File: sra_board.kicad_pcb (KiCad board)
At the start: 2 copper layers, 1 part, among them U2 ESP32-WROOM-32E

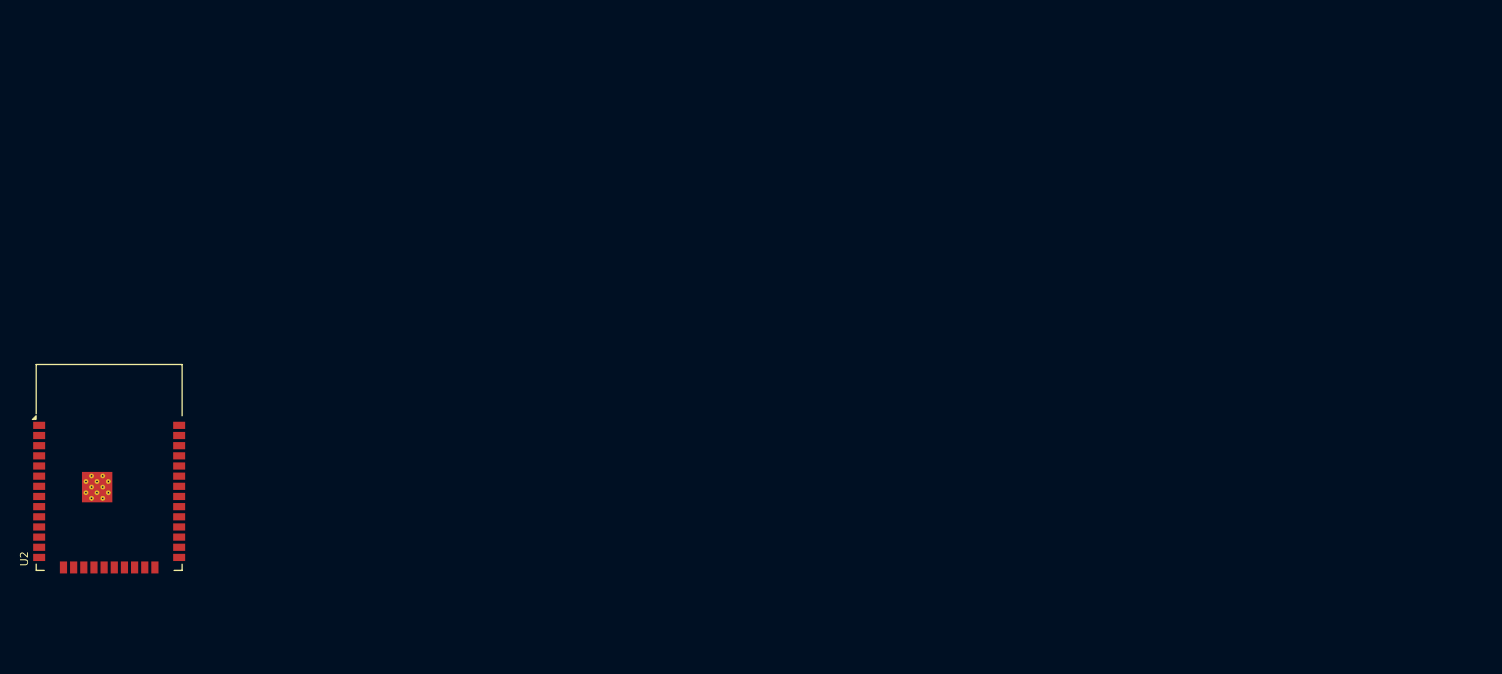
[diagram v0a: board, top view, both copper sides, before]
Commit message: Added Boot circuit and USB-to-TTL
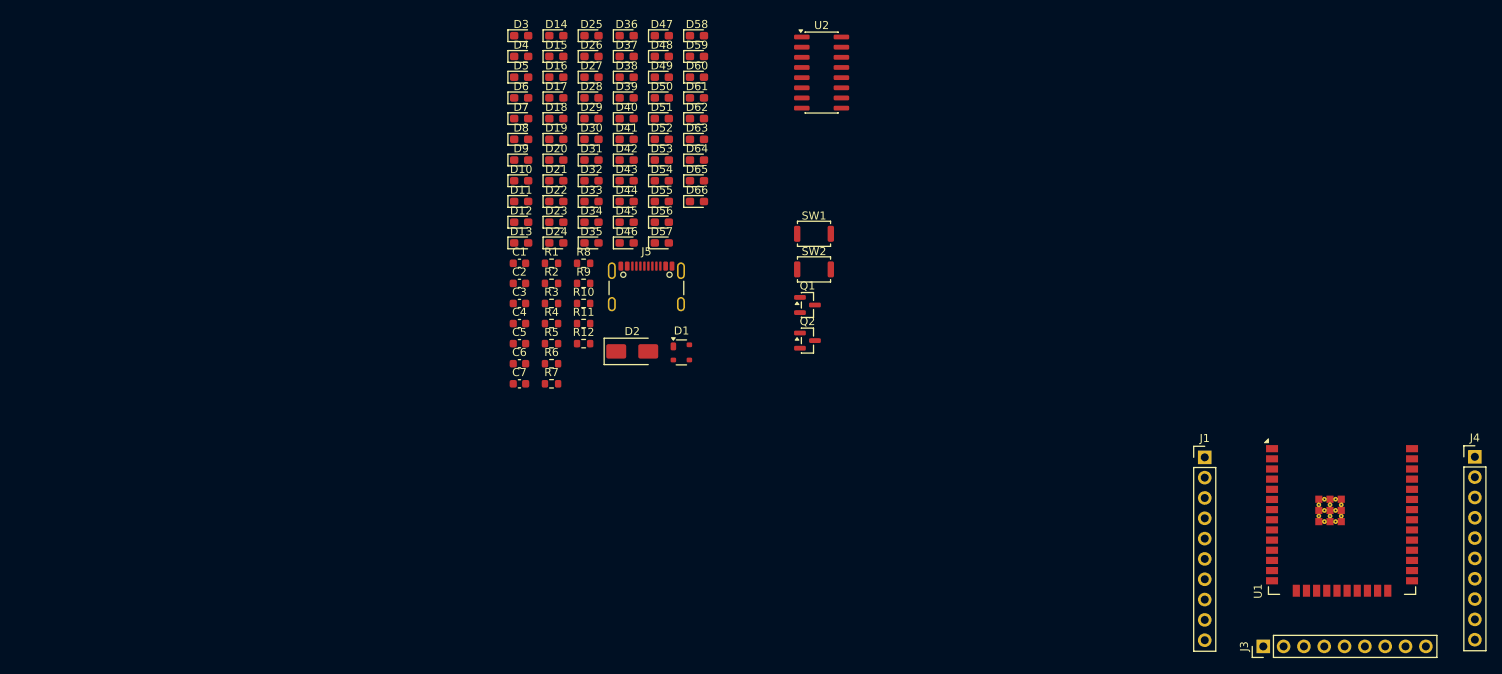
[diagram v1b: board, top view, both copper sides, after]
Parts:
- added C1: 0.1uf, Capacitor_SMD:C_0603_1608Metric, F.Cu at (105.5, 42.1)
- added C2: 0.1uF, Capacitor_SMD:C_0603_1608Metric, F.Cu at (105.5, 44.6)
- added C3: 0.1 uF, Capacitor_SMD:C_0603_1608Metric, F.Cu at (105.5, 47.1)
- added C4: 0.1uF, Capacitor_SMD:C_0603_1608Metric, F.Cu at (105.5, 49.6)
- added C5: 0.1uF, Capacitor_SMD:C_0603_1608Metric, F.Cu at (105.5, 52.1)
- added C6: 100nf, Capacitor_SMD:C_0603_1608Metric, F.Cu at (105.5, 54.6)
- added C7: 10uf, Capacitor_SMD:C_0603_1608Metric, F.Cu at (105.5, 57.1)
- added D1: SP0503BAHT, Package_TO_SOT_SMD:SOT-143, F.Cu at (125.7, 53.2)
- added D10: LED, LED_SMD:LED_0603_1608Metric_Pad1.05x0.95mm_HandSolder, F.Cu at (105.7, 31.7)
- added D11: LED, LED_SMD:LED_0603_1608Metric_Pad1.05x0.95mm_HandSolder, F.Cu at (105.7, 34.3)
- added D12: LED, LED_SMD:LED_0603_1608Metric_Pad1.05x0.95mm_HandSolder, F.Cu at (105.7, 36.9)
- added D13: LED, LED_SMD:LED_0603_1608Metric_Pad1.05x0.95mm_HandSolder, F.Cu at (105.7, 39.5)
- added D14: LED, LED_SMD:LED_0603_1608Metric_Pad1.05x0.95mm_HandSolder, F.Cu at (110.1, 13.6)
- added D15: LED, LED_SMD:LED_0603_1608Metric_Pad1.05x0.95mm_HandSolder, F.Cu at (110.1, 16.2)
- added D16: LED, LED_SMD:LED_0603_1608Metric_Pad1.05x0.95mm_HandSolder, F.Cu at (110.1, 18.8)
- added D17: LED, LED_SMD:LED_0603_1608Metric_Pad1.05x0.95mm_HandSolder, F.Cu at (110.1, 21.4)
- added D18: LED, LED_SMD:LED_0603_1608Metric_Pad1.05x0.95mm_HandSolder, F.Cu at (110.1, 24.0)
- added D19: LED, LED_SMD:LED_0603_1608Metric_Pad1.05x0.95mm_HandSolder, F.Cu at (110.1, 26.6)
- added D2: SS14, Diode_SMD:D_SMA, F.Cu at (119.6, 53.1)
- added D20: LED, LED_SMD:LED_0603_1608Metric_Pad1.05x0.95mm_HandSolder, F.Cu at (110.1, 29.2)
- added D21: LED, LED_SMD:LED_0603_1608Metric_Pad1.05x0.95mm_HandSolder, F.Cu at (110.1, 31.7)
- added D22: LED, LED_SMD:LED_0603_1608Metric_Pad1.05x0.95mm_HandSolder, F.Cu at (110.1, 34.3)
- added D23: LED, LED_SMD:LED_0603_1608Metric_Pad1.05x0.95mm_HandSolder, F.Cu at (110.1, 36.9)
- added D24: LED, LED_SMD:LED_0603_1608Metric_Pad1.05x0.95mm_HandSolder, F.Cu at (110.1, 39.5)
- added D25: LED, LED_SMD:LED_0603_1608Metric_Pad1.05x0.95mm_HandSolder, F.Cu at (114.5, 13.6)
- added D26: LED, LED_SMD:LED_0603_1608Metric_Pad1.05x0.95mm_HandSolder, F.Cu at (114.5, 16.2)
- added D27: LED, LED_SMD:LED_0603_1608Metric_Pad1.05x0.95mm_HandSolder, F.Cu at (114.5, 18.8)
- added D28: LED, LED_SMD:LED_0603_1608Metric_Pad1.05x0.95mm_HandSolder, F.Cu at (114.5, 21.4)
- added D29: LED, LED_SMD:LED_0603_1608Metric_Pad1.05x0.95mm_HandSolder, F.Cu at (114.5, 24.0)
- added D3: LED, LED_SMD:LED_0603_1608Metric_Pad1.05x0.95mm_HandSolder, F.Cu at (105.7, 13.6)
- added D30: LED, LED_SMD:LED_0603_1608Metric_Pad1.05x0.95mm_HandSolder, F.Cu at (114.5, 26.6)
- added D31: LED, LED_SMD:LED_0603_1608Metric_Pad1.05x0.95mm_HandSolder, F.Cu at (114.5, 29.2)
- added D32: LED, LED_SMD:LED_0603_1608Metric_Pad1.05x0.95mm_HandSolder, F.Cu at (114.5, 31.7)
- added D33: LED, LED_SMD:LED_0603_1608Metric_Pad1.05x0.95mm_HandSolder, F.Cu at (114.5, 34.3)
- added D34: LED, LED_SMD:LED_0603_1608Metric_Pad1.05x0.95mm_HandSolder, F.Cu at (114.5, 36.9)
- added D35: LED, LED_SMD:LED_0603_1608Metric_Pad1.05x0.95mm_HandSolder, F.Cu at (114.5, 39.5)
- added D36: LED, LED_SMD:LED_0603_1608Metric_Pad1.05x0.95mm_HandSolder, F.Cu at (118.9, 13.6)
- added D37: LED, LED_SMD:LED_0603_1608Metric_Pad1.05x0.95mm_HandSolder, F.Cu at (118.9, 16.2)
- added D38: LED, LED_SMD:LED_0603_1608Metric_Pad1.05x0.95mm_HandSolder, F.Cu at (118.9, 18.8)
- added D39: LED, LED_SMD:LED_0603_1608Metric_Pad1.05x0.95mm_HandSolder, F.Cu at (118.9, 21.4)
- added D4: LED, LED_SMD:LED_0603_1608Metric_Pad1.05x0.95mm_HandSolder, F.Cu at (105.7, 16.2)
- added D40: LED, LED_SMD:LED_0603_1608Metric_Pad1.05x0.95mm_HandSolder, F.Cu at (118.9, 24.0)
- added D41: LED, LED_SMD:LED_0603_1608Metric_Pad1.05x0.95mm_HandSolder, F.Cu at (118.9, 26.6)
- added D42: LED, LED_SMD:LED_0603_1608Metric_Pad1.05x0.95mm_HandSolder, F.Cu at (118.9, 29.2)
- added D43: LED, LED_SMD:LED_0603_1608Metric_Pad1.05x0.95mm_HandSolder, F.Cu at (118.9, 31.7)
- added D44: LED, LED_SMD:LED_0603_1608Metric_Pad1.05x0.95mm_HandSolder, F.Cu at (118.9, 34.3)
- added D45: LED, LED_SMD:LED_0603_1608Metric_Pad1.05x0.95mm_HandSolder, F.Cu at (118.9, 36.9)
- added D46: LED, LED_SMD:LED_0603_1608Metric_Pad1.05x0.95mm_HandSolder, F.Cu at (118.9, 39.5)
- added D47: LED, LED_SMD:LED_0603_1608Metric_Pad1.05x0.95mm_HandSolder, F.Cu at (123.3, 13.6)
- added D48: LED, LED_SMD:LED_0603_1608Metric_Pad1.05x0.95mm_HandSolder, F.Cu at (123.3, 16.2)
- added D49: LED, LED_SMD:LED_0603_1608Metric_Pad1.05x0.95mm_HandSolder, F.Cu at (123.3, 18.8)
- added D5: LED, LED_SMD:LED_0603_1608Metric_Pad1.05x0.95mm_HandSolder, F.Cu at (105.7, 18.8)
- added D50: LED, LED_SMD:LED_0603_1608Metric_Pad1.05x0.95mm_HandSolder, F.Cu at (123.3, 21.4)
- added D51: LED, LED_SMD:LED_0603_1608Metric_Pad1.05x0.95mm_HandSolder, F.Cu at (123.3, 24.0)
- added D52: LED, LED_SMD:LED_0603_1608Metric_Pad1.05x0.95mm_HandSolder, F.Cu at (123.3, 26.6)
- added D53: LED, LED_SMD:LED_0603_1608Metric_Pad1.05x0.95mm_HandSolder, F.Cu at (123.3, 29.2)
- added D54: LED, LED_SMD:LED_0603_1608Metric_Pad1.05x0.95mm_HandSolder, F.Cu at (123.3, 31.7)
- added D55: LED, LED_SMD:LED_0603_1608Metric_Pad1.05x0.95mm_HandSolder, F.Cu at (123.3, 34.3)
- added D56: LED, LED_SMD:LED_0603_1608Metric_Pad1.05x0.95mm_HandSolder, F.Cu at (123.3, 36.9)
- added D57: LED, LED_SMD:LED_0603_1608Metric_Pad1.05x0.95mm_HandSolder, F.Cu at (123.3, 39.5)
- added D58: LED, LED_SMD:LED_0603_1608Metric_Pad1.05x0.95mm_HandSolder, F.Cu at (127.7, 13.6)
- added D59: LED, LED_SMD:LED_0603_1608Metric_Pad1.05x0.95mm_HandSolder, F.Cu at (127.7, 16.2)
- added D6: LED, LED_SMD:LED_0603_1608Metric_Pad1.05x0.95mm_HandSolder, F.Cu at (105.7, 21.4)
- added D60: LED, LED_SMD:LED_0603_1608Metric_Pad1.05x0.95mm_HandSolder, F.Cu at (127.7, 18.8)
- added D61: LED, LED_SMD:LED_0603_1608Metric_Pad1.05x0.95mm_HandSolder, F.Cu at (127.7, 21.4)
- added D62: LED, LED_SMD:LED_0603_1608Metric_Pad1.05x0.95mm_HandSolder, F.Cu at (127.7, 24.0)
- added D63: LED, LED_SMD:LED_0603_1608Metric_Pad1.05x0.95mm_HandSolder, F.Cu at (127.7, 26.6)
- added D64: LED, LED_SMD:LED_0603_1608Metric_Pad1.05x0.95mm_HandSolder, F.Cu at (127.7, 29.2)
- added D65: LED, LED_SMD:LED_0603_1608Metric_Pad1.05x0.95mm_HandSolder, F.Cu at (127.7, 31.7)
- added D66: LED, LED_SMD:LED_0603_1608Metric_Pad1.05x0.95mm_HandSolder, F.Cu at (127.7, 34.3)
- added D7: LED, LED_SMD:LED_0603_1608Metric_Pad1.05x0.95mm_HandSolder, F.Cu at (105.7, 24.0)
- added D8: LED, LED_SMD:LED_0603_1608Metric_Pad1.05x0.95mm_HandSolder, F.Cu at (105.7, 26.6)
- added D9: LED, LED_SMD:LED_0603_1608Metric_Pad1.05x0.95mm_HandSolder, F.Cu at (105.7, 29.2)
- added J1: Conn_01x14_Pin, Connector_PinHeader_2.54mm:PinHeader_1x10_P2.54mm_Vertical, F.Cu at (191.1, 66.3)
- added J3: Conn_01x08_Pin, Connector_PinHeader_2.54mm:PinHeader_1x09_P2.54mm_Vertical, F.Cu at (198.5, 90.0)
- added J4: Conn_01x14_Pin, Connector_PinHeader_2.54mm:PinHeader_1x10_P2.54mm_Vertical, F.Cu at (224.9, 66.3)
- added J5: USB_C_Receptacle_USB2.0_16P, Connector_USB:USB_C_Receptacle_GCT_USB4105-xx-A_16P_TopMnt_Horizontal, F.Cu at (121.4, 46.1)
- added Q1: SS8050, Package_TO_SOT_SMD:SOT-23, F.Cu at (141.5, 47.3)
- added Q2: SS8050, Package_TO_SOT_SMD:SOT-23, F.Cu at (141.5, 51.7)
- added R1: 10k, Resistor_SMD:R_0603_1608Metric, F.Cu at (109.5, 42.1)
- added R10: 5.1K, Resistor_SMD:R_0603_1608Metric, F.Cu at (113.5, 47.1)
- added R11: 5.1K, Resistor_SMD:R_0603_1608Metric, F.Cu at (113.5, 49.6)
- added R12: 10k, Resistor_SMD:R_0603_1608Metric, F.Cu at (113.5, 52.1)
- added R2: 10K, Resistor_SMD:R_0603_1608Metric, F.Cu at (109.5, 44.6)
- added R3: 10K, Resistor_SMD:R_0603_1608Metric, F.Cu at (109.5, 47.1)
- added R4: 1k, Resistor_SMD:R_0603_1608Metric, F.Cu at (109.5, 49.6)
- added R5: 1k, Resistor_SMD:R_0603_1608Metric, F.Cu at (109.5, 52.1)
- added R6: 1k, Resistor_SMD:R_0603_1608Metric, F.Cu at (109.5, 54.6)
- added R7: 1k, Resistor_SMD:R_0603_1608Metric, F.Cu at (109.5, 57.1)
- added R8: 10K, Resistor_SMD:R_0603_1608Metric, F.Cu at (113.5, 42.1)
- added R9: 10K, Resistor_SMD:R_0603_1608Metric, F.Cu at (113.5, 44.6)
- added SW1: SW_0, Button_Switch_SMD:SW_Push_SPST_NO_Alps_SKRK, F.Cu at (142.3, 38.4)
- added SW2: SW_EN, Button_Switch_SMD:SW_Push_SPST_NO_Alps_SKRK, F.Cu at (142.3, 42.8)
- added U2: CH340C, Package_SO:SOIC-16_3.9x9.9mm_P1.27mm, F.Cu at (143.3, 18.2)
- U1: renamed from U2; footprint RF_Module:ESP32-WROOM-32D -> RF_Module:ESP32-WROOM-32E
- moved U1 154.1 mm to (208.3, 70.5)
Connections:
- U1 pad 29: /5 -> /CS
- U1 pad 30: /18 -> /CLK
- U1 pad 37: /23 -> /Din

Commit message: Adding power charging circuit for charging battery on seperate type-c
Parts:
- added C10: 0.1uF, Capacitor_SMD:C_0603_1608Metric, F.Cu at (161.2, 119.9)
- added C11: 10uF, Capacitor_SMD:C_0603_1608Metric, F.Cu at (161.2, 122.4)
- added C12: 10uF, Capacitor_SMD:C_0603_1608Metric, F.Cu at (161.2, 124.9)
- added C13: 22uF, Capacitor_SMD:C_0603_1608Metric, F.Cu at (161.2, 127.4)
- added C14: 22uF, Capacitor_SMD:C_0603_1608Metric, F.Cu at (161.2, 130.0)
- added C15: NC, Capacitor_SMD:C_0603_1608Metric, F.Cu at (161.2, 132.5)
- added C16: 0.1uF, Capacitor_SMD:C_0603_1608Metric, F.Cu at (161.2, 135.0)
- added C8: 22uF, Capacitor_SMD:C_0603_1608Metric, F.Cu at (264.8, 150.2)
- added C9: 22uF, Capacitor_SMD:C_0603_1608Metric, F.Cu at (264.8, 152.7)
- added D67: LED, LED_SMD:LED_0603_1608Metric_Pad1.05x0.95mm_HandSolder, F.Cu at (278.6, 150.2)
- added D68: SS34, Diode_SMD:D_SMA, F.Cu at (270.9, 157.1)
- added D69: LED, LED_SMD:LED_0603_1608Metric_Pad1.05x0.95mm_HandSolder, F.Cu at (278.6, 152.8)
- added D70: SS34, Diode_SMD:D_SMA, F.Cu at (270.9, 161.6)
- added D71: SS34, Diode_SMD:D_SMB, F.Cu at (178.9, 134.7)
- added D72: SMBJ5.0A, Diode_SMD:D_SMB, F.Cu at (178.9, 140.3)
- added D73: SS34, Diode_SMD:D_SMB, F.Cu at (178.9, 145.8)
- added D74: LED, LED_SMD:LED_0603_1608Metric_Pad1.05x0.95mm_HandSolder, F.Cu at (165.4, 141.8)
- added D75: SS14, Diode_SMD:D_SMA, F.Cu at (187.1, 143.5)
- added D76: LED, LED_SMD:LED_0603_1608Metric_Pad1.05x0.95mm_HandSolder, F.Cu at (165.4, 144.4)
- added F1: 3A, Fuse:Fuse_Littelfuse-LVR100, F.Cu at (179.1, 122.0)
- added F2: 1A, Fuse:Fuse_Littelfuse-LVR100, F.Cu at (179.1, 128.6)
- added J2: USB_C_Receptacle_PowerOnly_6P, Connector_USB:USB_C_Receptacle_GCT_USB4125-xx-x-0190_6P_TopMnt_Horizontal, F.Cu at (189.0, 136.8)
- added J6: B2B-XH-A_LF__SN_, Connector_JST:JST_EH_B2B-EH-A_1x02_P2.50mm_Vertical, F.Cu at (270.3, 151.6)
- added Q3: AO3400A, Package_TO_SOT_SMD:SOT-23, F.Cu at (277.3, 157.0)
- added Q4: AO3401A, Package_TO_SOT_SMD:SOT-23, F.Cu at (277.3, 161.5)
- added R14: 1k, Resistor_SMD:R_0603_1608Metric, F.Cu at (264.8, 155.2)
- added R15: 1k, Resistor_SMD:R_0603_1608Metric, F.Cu at (264.8, 157.7)
- added R16: 5.1K, Resistor_SMD:R_0603_1608Metric, F.Cu at (161.2, 140.0)
- added SW3: SW_Push_DPDT, Button_Switch_THT:SW_Push_2P2T_Toggle_CK_PVA2OAH5xxxxxxV2, F.Cu at (166.5, 121.2)
- added SW4: SW_Push_DPDT, Button_Switch_THT:SW_Push_2P2T_Toggle_CK_PVA2OAH5xxxxxxV2, F.Cu at (166.5, 132.1)
- added U5: CN3302, easyeda2kicad:SOP-8_L4.9-W3.9-P1.27-LS6.0-BL, F.Cu at (258.7, 82.2)
- added U6: TPS562202, Package_TO_SOT_SMD:SOT-563, F.Cu at (169.3, 142.2)
- R9: value 10K -> 5.1K
- moved R9 104.4 mm to (161.2, 137.5)
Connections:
- C6 pad 1: /5V -> /5v
- C7 pad 1: /5V -> /5v
- D2 pad 1: /5V_P -> /5v
- R9 pad 1: /EN -> Net-(J2-CC1)
- R9 pad 2: /3V3 -> GND

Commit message: Using only one type c
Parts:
- removed C1: 0.1uf, Capacitor_SMD:C_0603_1608Metric
- removed D71: SS34, Diode_SMD:D_SMB
- removed D72: SMBJ5.0A, Diode_SMD:D_SMB
- removed J2: USB_C_Receptacle_PowerOnly_6P, Connector_USB:USB_C_Receptacle_GCT_USB4125-xx-x-0190_6P_TopMnt_Horizontal
- removed R1, R12: 10k, Resistor_SMD:R_0603_1608Metric
- removed R16, R9: 5.1K, Resistor_SMD:R_0603_1608Metric
- removed U1: ESP32-WROOM-32E, RF_Module:ESP32-WROOM-32E
- added C17: 1uf, Capacitor_SMD:C_0805_2012Metric, F.Cu at (134.6, 85.7)
- added C18: 1uf, Capacitor_SMD:C_0805_2012Metric, F.Cu at (134.6, 88.2)
- added C19: 0.1uf, Capacitor_SMD:C_0603_1608Metric, F.Cu at (134.6, 90.7)
- added J10: Conn_01x03_Pin, Connector_PinHeader_2.54mm:PinHeader_1x03_P2.54mm_Vertical, F.Cu at (130.3, 77.0)
- added J11: Conn_01x03_Pin, Connector_PinHeader_2.54mm:PinHeader_1x03_P2.54mm_Vertical, F.Cu at (134.9, 77.0)
- added J12: Conn_01x03_Pin, Connector_PinHeader_2.54mm:PinHeader_1x03_P2.54mm_Vertical, F.Cu at (139.5, 77.0)
- added J13: Conn_01x08_Pin, Connector_PinHeader_2.54mm:PinHeader_1x08_P2.54mm_Vertical, F.Cu at (125.8, 86.7)
- added J14: Conn_01x07_Pin, Connector_PinHeader_2.54mm:PinHeader_1x07_P2.54mm_Vertical, F.Cu at (130.3, 86.7)
- added J15: Conn_01x04_Pin, Connector_PinHeader_2.54mm:PinHeader_1x04_P2.54mm_Vertical, F.Cu at (147.0, 86.7)
- added J16: Conn_01x03_Pin, Connector_PinHeader_2.54mm:PinHeader_1x03_P2.54mm_Vertical, F.Cu at (144.1, 77.0)
- added J17: Conn_01x03_Pin, Connector_PinHeader_2.54mm:PinHeader_1x03_P2.54mm_Vertical, F.Cu at (148.7, 77.0)
- added J18: Conn_01x03_Pin, Connector_PinHeader_2.54mm:PinHeader_1x03_P2.54mm_Vertical, F.Cu at (153.3, 77.0)
- added J7: B2B-XH-A_LF__SN_, Connector_JST:JST_EH_B2B-EH-A_1x02_P2.50mm_Vertical, F.Cu at (100.5, 144.9)
- added J8: B2B-XH-A_LF__SN_, Connector_JST:JST_EH_B2B-EH-A_1x02_P2.50mm_Vertical, F.Cu at (100.5, 150.7)
- added J9: Conn_01x03_Pin, Connector_PinHeader_2.54mm:PinHeader_1x03_P2.54mm_Vertical, F.Cu at (125.8, 77.0)
- added L1: 4.7uH, Inductor_SMD:L_Sunlord_MWSA0402S, F.Cu at (69.8, 122.5)
- added L2: 4.7uH, Inductor_SMD:L_Sunlord_MWSA0402S, F.Cu at (152.6, 93.0)
- added R13: 47m, Resistor_SMD:R_0805_2012Metric, F.Cu at (46.1, 111.5)
- added R17: 10k, Resistor_SMD:R_0805_2012Metric, F.Cu at (134.6, 95.7)
- added R18: 10k, Resistor_SMD:R_0805_2012Metric, F.Cu at (138.7, 85.7)
- added R19: 52k3, Resistor_SMD:R_0805_2012Metric, F.Cu at (138.7, 88.2)
- added R20: 330, Resistor_SMD:R_0603_1608Metric, F.Cu at (138.7, 90.7)
- added R21: R, Resistor_SMD:R_0603_1608Metric, F.Cu at (138.7, 93.2)
- added R22: R, Resistor_SMD:R_0603_1608Metric, F.Cu at (138.7, 95.7)
- added R23: 10k, Resistor_SMD:R_0603_1608Metric, F.Cu at (142.7, 85.7)
- added R24: 10k, Resistor_SMD:R_0603_1608Metric, F.Cu at (142.7, 88.2)
- added R50: 680, Resistor_SMD:R_0603_1608Metric, F.Cu at (142.7, 90.7)
- added U7: ME6211C33M5, Package_TO_SOT_SMD:SOT-23-5, F.Cu at (109.1, 144.7)
- added U8: ESP32-WROOM-32E, RF_Module:ESP32-WROOM-32D, F.Cu at (208.4, 73.2)
- C10, C11, C12, C13, C14, C15, C16: footprint Capacitor_SMD:C_0603_1608Metric -> Capacitor_SMD:C_0805_2012Metric
- C8, C9: value 22uF -> 33uF; footprint Capacitor_SMD:C_0603_1608Metric -> Capacitor_SMD:C_1206_3216Metric
- R14, R15: footprint Resistor_SMD:R_0603_1608Metric -> Resistor_SMD:R_0805_2012Metric
- SW3, SW4: value SW_Push_DPDT -> Switch
- moved Q4 235.0 mm to (48.4, 108.6), turned to -90 degrees
- moved Q3 227.0 mm to (50.8, 142.5)
- moved C8 227.0 mm to (38.3, 135.7)
- moved D68 227.0 mm to (44.3, 142.5)
- moved D70 227.0 mm to (44.3, 147.1)
- moved R14 227.0 mm to (38.3, 140.7)
- moved R15 227.0 mm to (38.3, 143.2)
- moved D67 227.0 mm to (52.0, 135.7)
- moved C9 220.6 mm to (45.0, 133.9)
- moved D69 217.9 mm to (61.5, 134.0)
- moved U5 214.5 mm to (47.1, 117.7)
- moved U6 13.6 mm to (168.4, 155.7)
- moved J3 2.19 mm to (198.5, 87.8)
- moved J1 1.81 mm to (192.9, 65.8)
- moved J4 0.63 mm to (224.3, 66.0)
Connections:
- C6 pad 1: /5v -> /5V_P
- C7 pad 1: /5v -> /5V_P
- C8 pad 2: /CE_CN3302 -> /5V_P_USB
- D2 pad 1: /5v -> /5V_P_USB
- D75 pad 1: Net-(D75-K) -> /5V_P_USB
- D76 pad 2: /5v -> /5V_P
- F2 pad 1: Net-(D75-K) -> /5V_P_USB
- R14 pad 2: /CE_CN3302 -> /5V_P_USB
- SW4 pad 3: /5v -> /5V_P
- SW4 pad 6: /5v -> /5V_P
- U5 pad 2: /CE_CN3302 -> /5V_P_USB
- U5 pad 7: /CE_CN3302 -> /5V_P_USB

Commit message: placed half components
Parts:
- added ?: , , F.Cu at (220.5, 116.9)
- added ?: , , F.Cu at (137.7, 34.1)
- added ?: , , F.Cu at (137.8, 116.9)
- added ?: , , F.Cu at (220.4, 34.1)
- added H5: MountingHole, MountingHole:MountingHole_2.1mm, F.Cu at (285.4, 68.4)
- added H6: MountingHole, MountingHole:MountingHole_2.1mm, F.Cu at (300.3, 68.3)
- added JP1: SolderBridge, Jumper:SolderJumper-2_P1.3mm_Open_RoundedPad1.0x1.5mm, F.Cu at (177.4, 88.3)
- added JP2: SolderBridge, Jumper:SolderJumper-2_P1.3mm_Open_RoundedPad1.0x1.5mm, F.Cu at (209.9, 88.6)
- added JP3: SolderBridge, Jumper:SolderJumper-2_P1.3mm_Open_RoundedPad1.0x1.5mm, F.Cu at (213.0, 88.6)
- added JP4: SolderBridge, Jumper:SolderJumper-2_P1.3mm_Open_RoundedPad1.0x1.5mm, F.Cu at (190.4, 43.0)
- added JP5: SolderBridge, Jumper:SolderJumper-2_P1.3mm_Open_RoundedPad1.0x1.5mm, F.Cu at (194.6, 43.1)
- added Q5: AO3401A, Package_TO_SOT_SMD:SOT-23, F.Cu at (177.7, 92.1)
- added Q6: AO3401A, Package_TO_SOT_SMD:SOT-23, F.Cu at (215.3, 84.0)
- added Q7: AO3401A, Package_TO_SOT_SMD:SOT-23, F.Cu at (193.5, 39.4)
- added R1: 100K, Resistor_SMD:R_0805_2012Metric, F.Cu at (177.5, 85.2)
- added R12: 100K, Resistor_SMD:R_0805_2012Metric, F.Cu at (189.8, 39.4)
- added R9: 100K, Resistor_SMD:R_0805_2012Metric, F.Cu at (215.0, 80.4)
- added SW5: SW_Wuerth_450301014042, Button_Switch_SMD:SW_SPDT_Shouhan_MSK12C02, F.Cu at (220.7, 82.1)
- added SW6: SW_Wuerth_450301014042, Button_Switch_SMD:SW_SPDT_Shouhan_MSK12C02, F.Cu at (191.9, 33.8)
- added U1: MAX7219CWG_T, footprints:SOIC24, F.Cu at (49.4, 27.2)
- added U3: TB6612FNG H-bridge Motor Driver, footprints:MODULE_ROB-14450, F.Cu at (191.4, 91.0)
- C2, C3, C4, C5, C6, C7: footprint Capacitor_SMD:C_0603_1608Metric -> Capacitor_SMD:C_0805_2012Metric
- D10, D11, D12, D13, D14, D15, D16, D17, D18, D19, D20, D21, D22, D23, D24, D25, D26, D27, D28, D29, D3, D30, D31, D32, D33, D34, D35, D36, D37, D38, D39, D4, D40, D41, D42, D43, D44, D45, D46, D47, D48, D49, D5, D50, D51, D52, D53, D54, D55, D56, D57, D58, D59, D6, D60, D61, D62, D63, D64, D65, D66, D7, D8, D9: footprint LED_SMD:LED_0603_1608Metric_Pad1.05x0.95mm_HandSolder -> LED_SMD:LED_0805_2012Metric
- D2: value SS14 -> SS34; footprint Diode_SMD:D_SMA -> Diode_SMD:D_SMB
- F1, F2: footprint Fuse:Fuse_Littelfuse-LVR100 -> Fuse:Fuse_2920_7451Metric
- J13: value Conn_01x08_Pin -> MPU0650; footprint Connector_PinHeader_2.54mm:PinHeader_1x08_P2.54mm_Vertical -> Connector_PinSocket_2.54mm:PinSocket_1x08_P2.54mm_Vertical
- J14: value Conn_01x07_Pin -> LSA; footprint Connector_PinHeader_2.54mm:PinHeader_1x07_P2.54mm_Vertical -> Connector_PinSocket_2.54mm:PinSocket_1x08_P2.54mm_Vertical
- J15: value Conn_01x04_Pin -> OLED; footprint Connector_PinHeader_2.54mm:PinHeader_1x04_P2.54mm_Vertical -> Connector_PinSocket_2.54mm:PinSocket_1x04_P2.54mm_Vertical
- L1, L2: footprint Inductor_SMD:L_Sunlord_MWSA0402S -> Inductor_SMD:L_Sunlord_MWSA0603S
- R10, R11, R2, R20, R21, R22, R23, R24, R3, R4, R5, R50, R6, R7, R8: footprint Resistor_SMD:R_0603_1608Metric -> Resistor_SMD:R_0805_2012Metric
- moved D70 192.6 mm to (218.4, 64.6), turned to 90 degrees
- moved R15 186.1 mm to (211.7, 76.0), turned to -90 degrees
- moved C8 185.0 mm to (211.7, 71.5), turned to 90 degrees
- moved R14 183.3 mm to (208.2, 72.1)
- moved C9 180.8 mm to (214.7, 71.5), turned to -90 degrees
- moved J13 178.4 mm to (301.7, 57.2), turned to -90 degrees
- moved D68 175.8 mm to (201.7, 64.1), turned to -90 degrees
- moved Q3 173.5 mm to (206.6, 66.2)
- moved U5 173.4 mm to (212.3, 64.8)
- moved R13 173.3 mm to (211.1, 58.6)
- moved D67 169.6 mm to (208.2, 69.6), turned to 180 degrees
- moved Q4 165.1 mm to (206.6, 61.3), turned to 180 degrees
- moved D69 163.8 mm to (214.7, 76.0), turned to 90 degrees
- moved R22 163.7 mm to (299.1, 63.3), turned to 180 degrees
- moved R21 163.6 mm to (299.1, 61.2), turned to 180 degrees
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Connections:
- C10 pad 1: /7v4 -> /VTPS
- C11 pad 1: /7v4 -> /VTPS
- C12 pad 1: /7v4 -> /VTPS
- F1 pad 2: Net-(F1-Pad2) -> /7V4_Switch
- F2 pad 2: Net-(F2-Pad2) -> /5V_Switch
- J15 pad 3: /22 -> /21
- J15 pad 4: /21 -> /22
- J3 pad 9: /IO0 -> /0
- R17 pad 1: /7v4 -> /VTPS
- SW3 pad 2: Net-(F1-Pad2) -> Net-(JP2-B)
- SW3 pad 5: Net-(F1-Pad2) -> Net-(JP2-B)
- SW4 pad 2: Net-(F2-Pad2) -> Net-(JP5-B)
- SW4 pad 5: Net-(F2-Pad2) -> Net-(JP5-B)
- U6 pad 1: /7v4 -> /VTPS
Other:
- board outline added: 70 x 70 mm

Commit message: rough placing of components
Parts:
- removed ? (x4): , 
- C8, C9: value 33uF -> 22uF
- R13: value 47m -> 40m
- U5: value CN3302 -> CN3303
- moved J4 181.0 mm to (135.0, 47.9), turned to 90 degrees
- moved C2 172.1 mm to (210.8, 52.2)
- moved U8 158.6 mm to (142.6, 61.9), turned to 90 degrees
- moved J1 155.6 mm to (134.9, 75.4), turned to 90 degrees
- moved C3 154.4 mm to (193.0, 56.6), turned to 180 degrees
- moved R2 144.5 mm to (188.3, 61.8), turned to 180 degrees
- moved R3 144.4 mm to (188.3, 65.1), turned to 180 degrees
- moved C4 142.4 mm to (180.5, 57.5), turned to -90 degrees
- moved C6 141.3 mm to (170.8, 35.9), turned to -90 degrees
- moved C5 140.6 mm to (180.5, 70.0), turned to 90 degrees
- moved C7 139.7 mm to (168.0, 35.9), turned to -90 degrees
- moved J13 138.2 mm to (163.9, 48.1), turned to 0 degrees
- moved R8 136.6 mm to (184.1, 57.5), turned to 90 degrees
- moved J3 133.7 mm to (157.2, 71.8), turned to 180 degrees
- moved R21 131.7 mm to (167.9, 50.7), turned to -90 degrees
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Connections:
- U1 pad 19: /5V -> /5V_P
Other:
- board size 70 x 70 mm -> 90 x 86.8 mm
- board text added: "Buck converter circuit"
- board text added: "CN3303 circuit"
- board text added: "Switch 12v"
- board text added: "Switch 5v"
- board text added: "USB circuit"
